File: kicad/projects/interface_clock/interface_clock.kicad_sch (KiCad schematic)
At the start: 76 parts, among them J1 Control_signal_backplane, J10 Power, J2 Aux_connection, J3 Bus_connection, J4 ADDRESS IN, J5 EXT BUS, J6 CTL SIGS IN, J7 SIG_TO_PERIPH, J8 EXT ADDR, J9 LED CTL, U1 74HC02, U10 74HC157, U11 74HC14, U12 74HC245, U13 74HC126, U14 74HC109, U2 74HC04, U3 74HC08, U5 74HC02, U6 74HC245, U7 74HC245, U8 74HC245, U9 74HC245, X1 CXO_DIP8

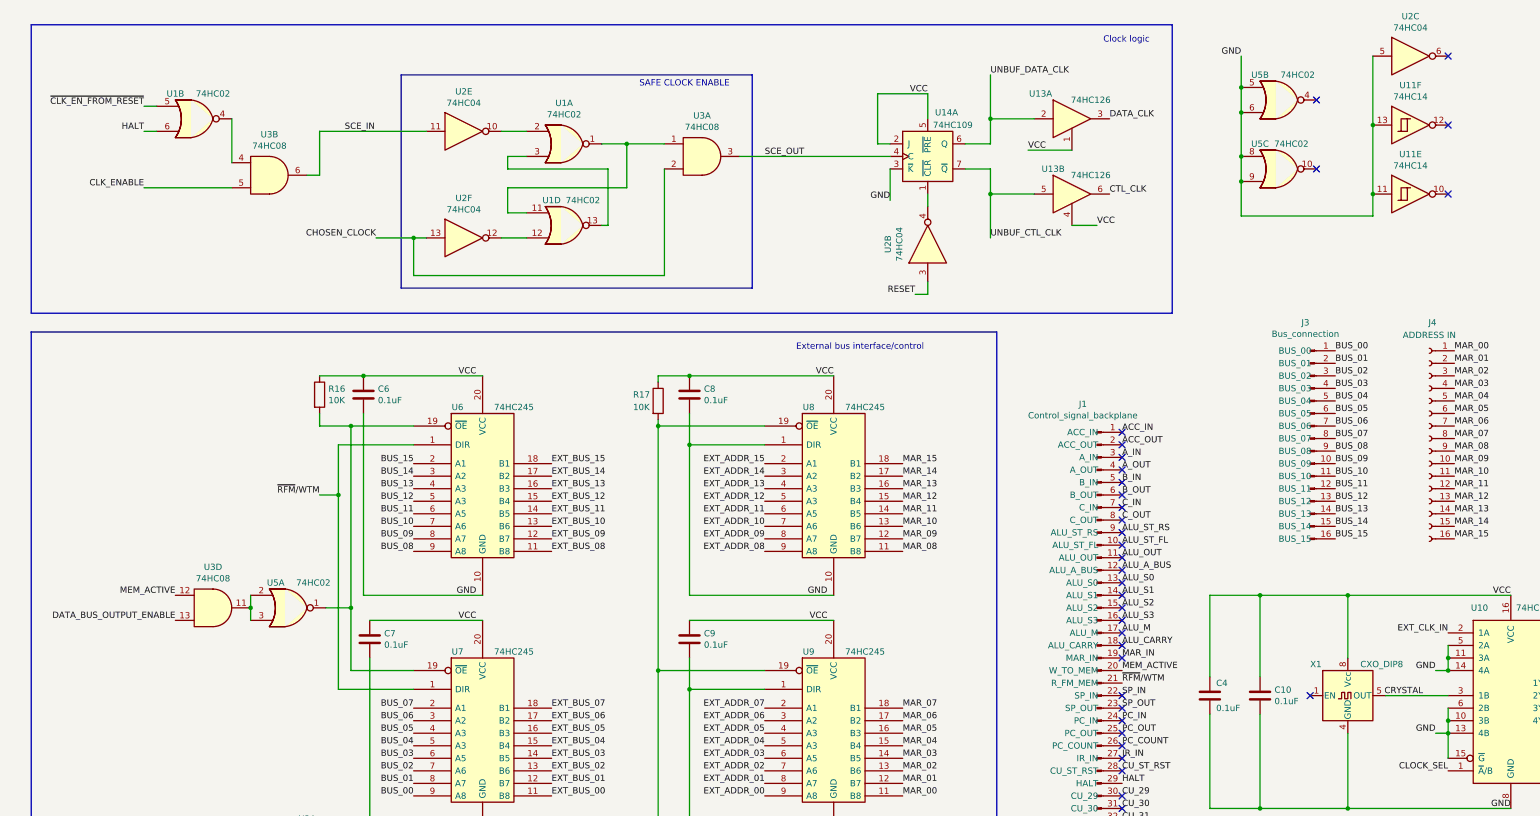
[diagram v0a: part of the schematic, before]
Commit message: Update interface clock to allow reading of databus when databus output is disabled.
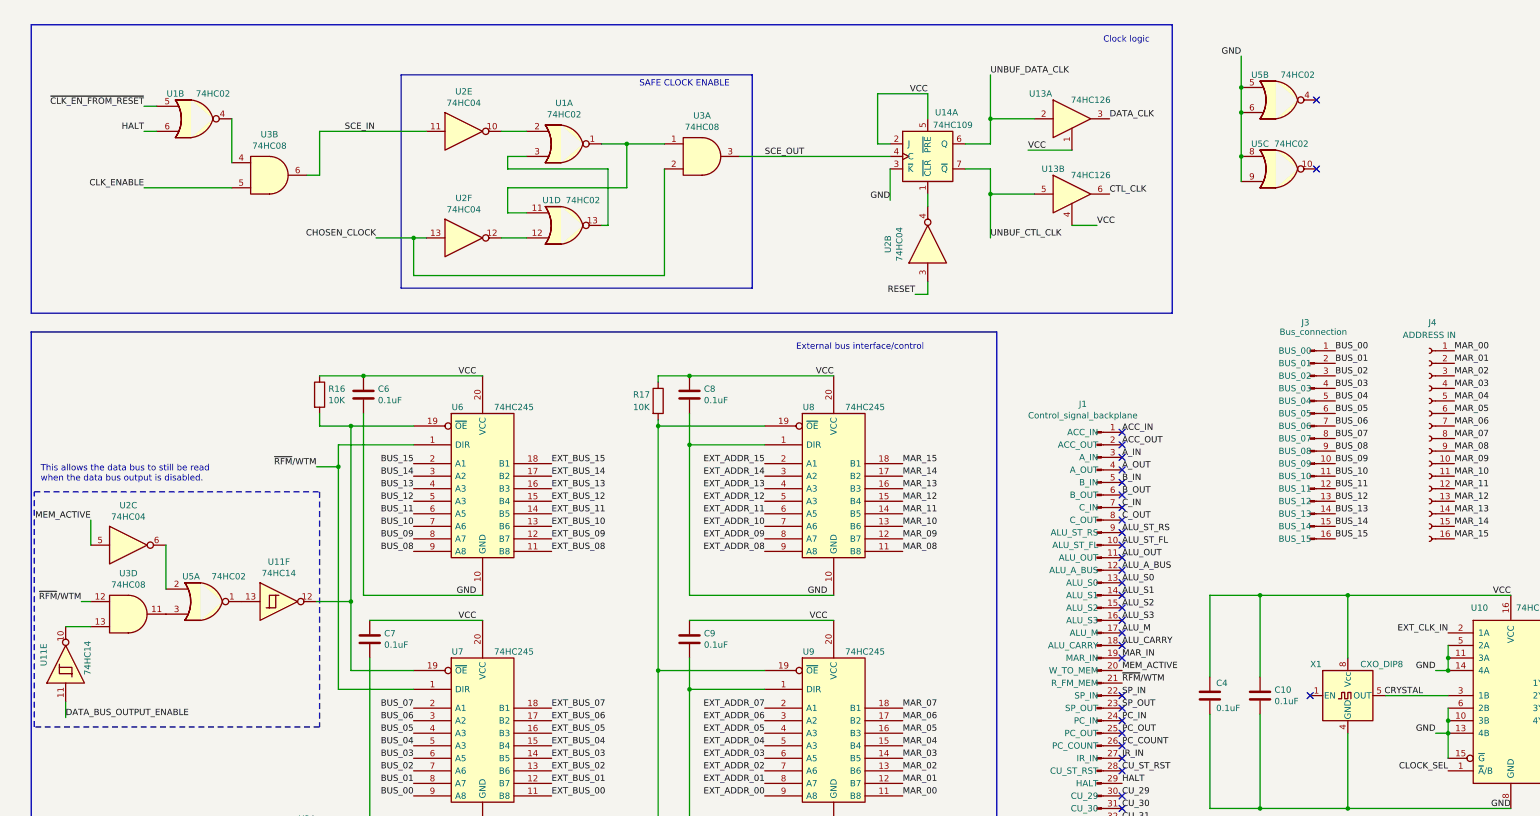
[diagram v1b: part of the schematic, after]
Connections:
- net DATA_BUS_OUTPUT_ENABLE: now also U11.11; no longer U3.13
- net GND: no longer U11.11, U11.13, U2.5
- net MEM_ACTIVE: now also U2.5; no longer U3.12
- net ~{RFM}/WTM: now also U3.12
- net at U2.6: now also U5.2
- net at R16.2, U6.19 (~{OE}), U7.19 (~{OE}): now also U11.12; no longer U5.1
- net at U3.11, U5.3: no longer U5.2
- net at U11.10: now also U3.13
- new net: U11.13, U5.1
- no-connect marks 44 -> 41
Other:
- note added: "This allows the data bus to still be read when the data bus output is disabled."
- moved on the sheet: U11E, U11F, U2C, U3D, U5A

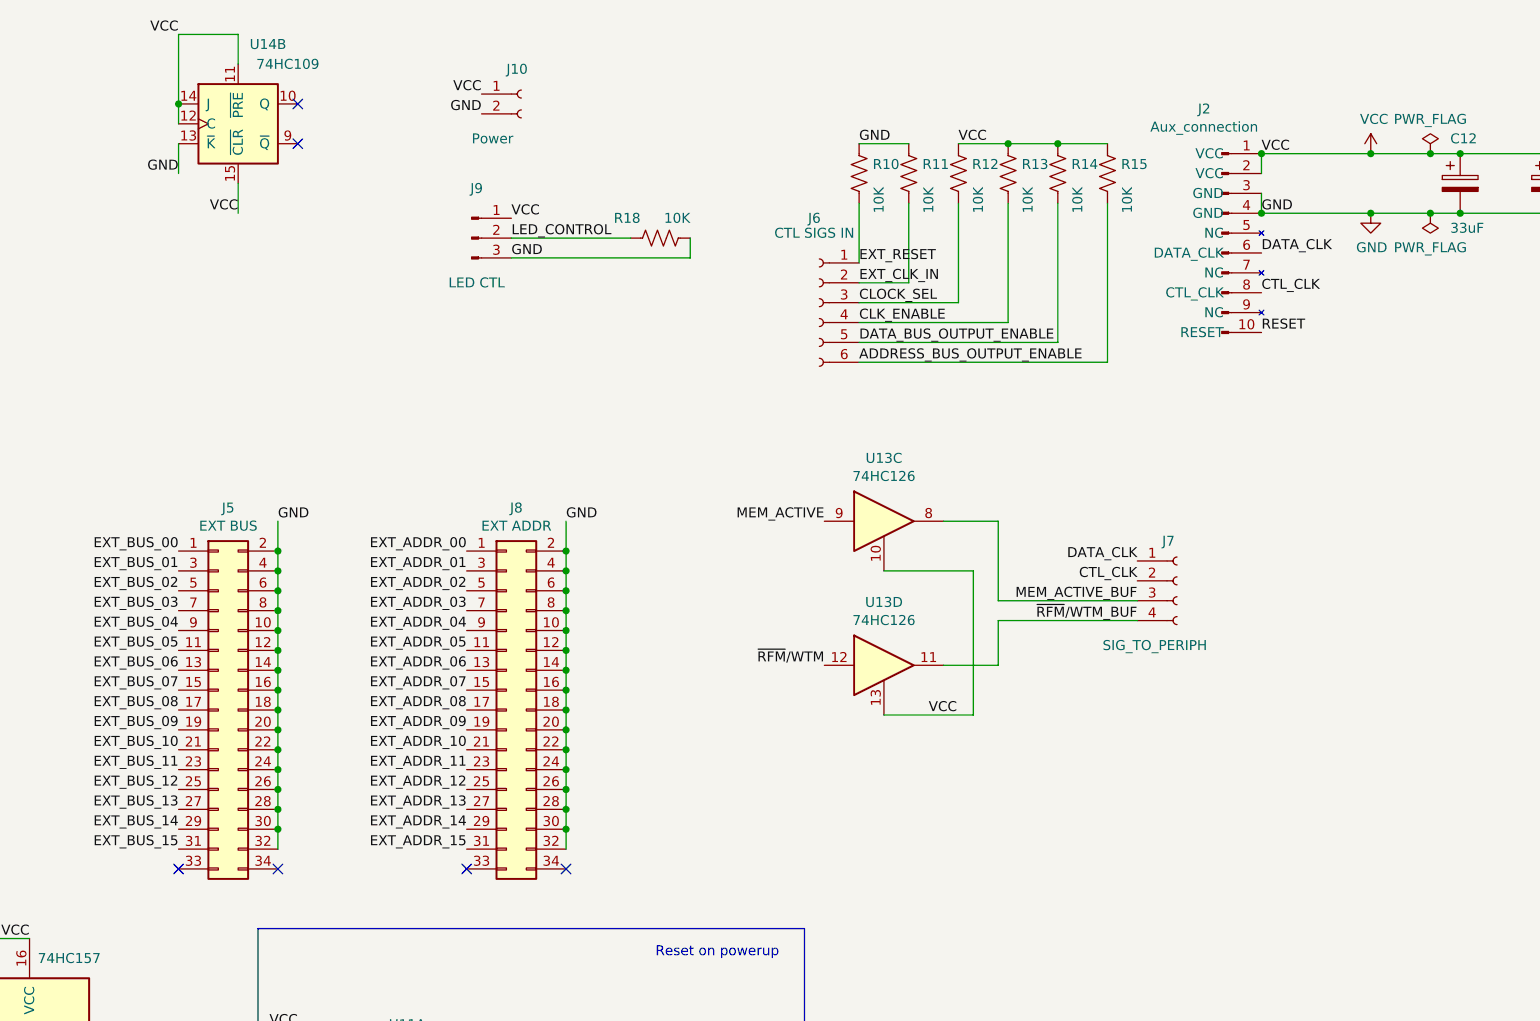
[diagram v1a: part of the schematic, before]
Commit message: Mid way through CPU interface bus connection redesign.
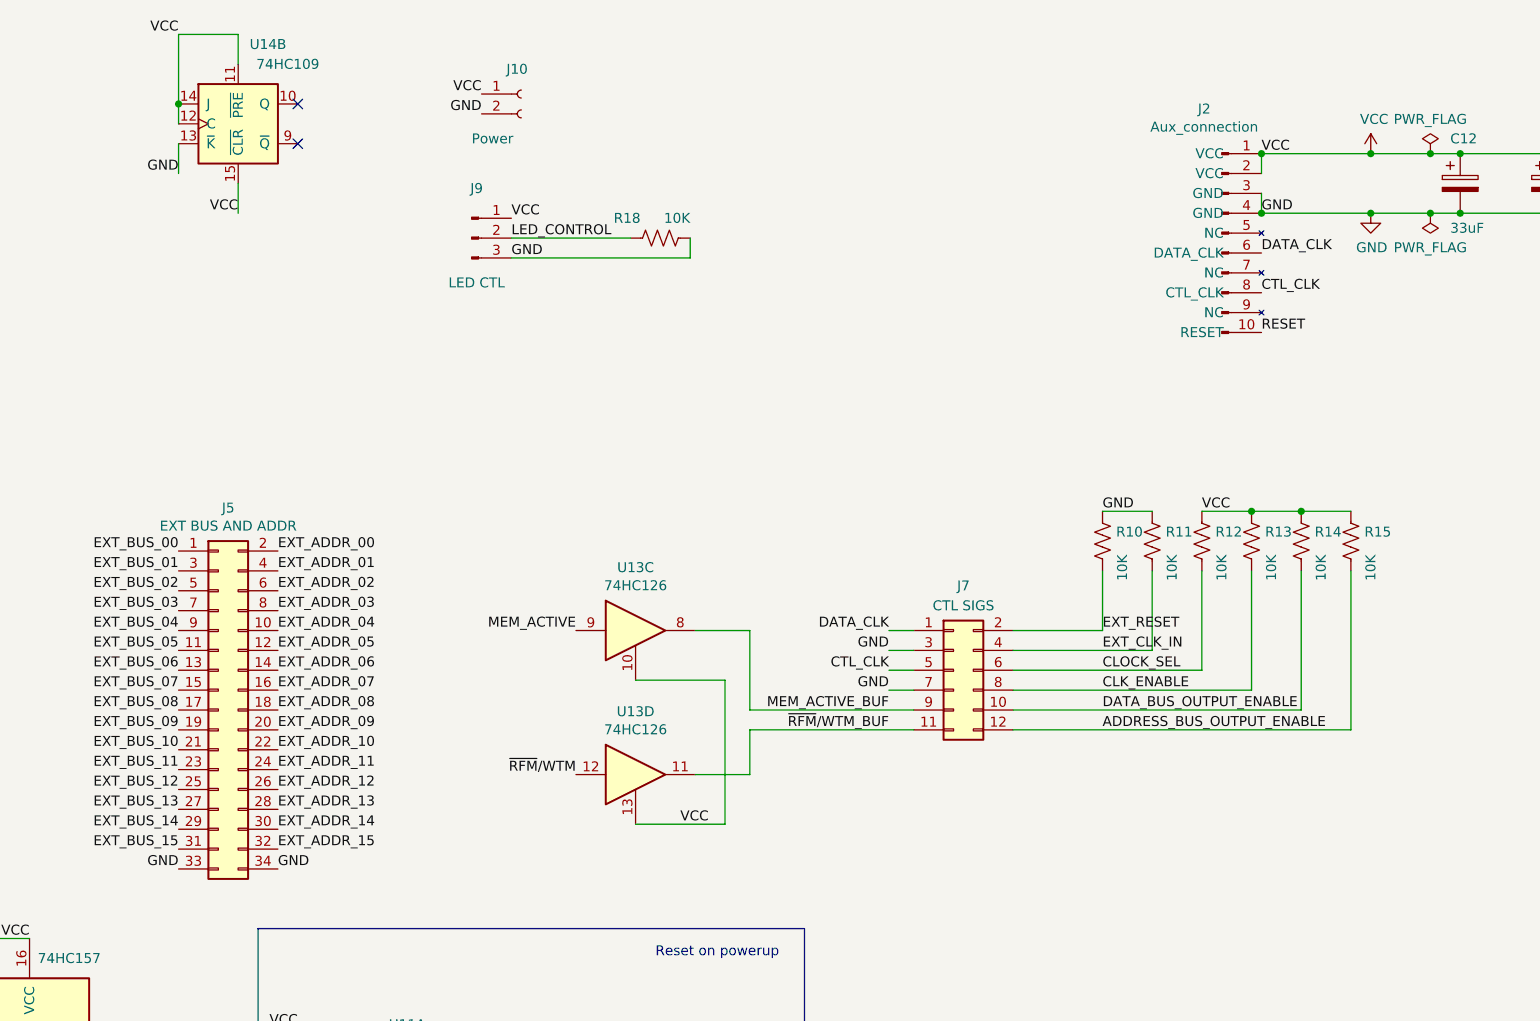
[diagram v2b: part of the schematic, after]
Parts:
- removed J6: CTL SIGS IN, Connector_PinSocket_2.54mm:PinSocket_1x06_P2.54mm_Horizontal, symbol Connector:Conn_01x06_Socket
- removed J7: SIG_TO_PERIPH, Connector_PinSocket_2.54mm:PinSocket_1x04_P2.54mm_Horizontal, symbol Connector:Conn_01x04_Socket
- removed J8: EXT ADDR, Connector_PinHeader_2.54mm:PinHeader_2x17_P2.54mm_Vertical, symbol Connector_Generic:Conn_02x17_Odd_Even
- added J7: CTL SIGS, Connector_PinSocket_2.54mm:PinSocket_2x06_P2.54mm_Horizontal, symbol Connector_Generic:Conn_02x06_Odd_Even
- J5: value EXT BUS -> EXT BUS AND ADDR; footprint Connector_PinHeader_2.54mm:PinHeader_2x17_P2.54mm_Vertical -> Connector_PinSocket_2.54mm:PinSocket_2x17_P2.54mm_Horizontal
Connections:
- net ADDRESS_BUS_OUTPUT_ENABLE: now also J7.12 (Pin_12)
- net CLK_ENABLE: now also J7.8 (Pin_8)
- net CLOCK_SEL: now also J7.6 (Pin_6)
- net CTL_CLK: now also J7.5 (Pin_5)
- net DATA_BUS_OUTPUT_ENABLE: now also J7.10 (Pin_10)
- net DATA_CLK: now also J7.1 (Pin_1)
- net EXT_ADDR_00: now also J5.2 (Pin_2)
- net EXT_ADDR_01: now also J5.4 (Pin_4)
- net EXT_ADDR_02: now also J5.6 (Pin_6)
- net EXT_ADDR_03: now also J5.8 (Pin_8)
- net EXT_ADDR_04: now also J5.10 (Pin_10)
- net EXT_ADDR_05: now also J5.12 (Pin_12)
- net EXT_ADDR_06: now also J5.14 (Pin_14)
- net EXT_ADDR_07: now also J5.16 (Pin_16)
- net EXT_ADDR_08: now also J5.18 (Pin_18)
- net EXT_ADDR_09: now also J5.20 (Pin_20)
- net EXT_ADDR_10: now also J5.22 (Pin_22)
- net EXT_ADDR_11: now also J5.24 (Pin_24)
- net EXT_ADDR_12: now also J5.26 (Pin_26)
- net EXT_ADDR_13: now also J5.28 (Pin_28)
- net EXT_ADDR_14: now also J5.30 (Pin_30)
- net EXT_ADDR_15: now also J5.32 (Pin_32)
- net EXT_CLK_IN: now also J7.4 (Pin_4)
- net EXT_RESET: now also J7.2 (Pin_2)
- net GND: now also J5.33 (Pin_33), J5.34 (Pin_34), J7.3 (Pin_3), J7.7 (Pin_7); no longer J5.10 (Pin_10), J5.12 (Pin_12), J5.14 (Pin_14), J5.16 (Pin_16), J5.18 (Pin_18), J5.2 (Pin_2), J5.20 (Pin_20), J5.22 (Pin_22), J5.24 (Pin_24), J5.26 (Pin_26), J5.28 (Pin_28), J5.30 (Pin_30), J5.32 (Pin_32), J5.4 (Pin_4), J5.6 (Pin_6), J5.8 (Pin_8)
- net MEM_ACTIVE_BUF: now also J7.9 (Pin_9)
- net ~{RFM}/WTM_BUF: now also J7.11 (Pin_11)
- no-connect marks 41 -> 37
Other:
- moved on the sheet: R10, R11, R12, R13, R14, R15, U13C, U13D
